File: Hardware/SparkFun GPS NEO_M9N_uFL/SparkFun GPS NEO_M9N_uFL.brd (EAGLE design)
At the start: 40.6 x 33 mm, 93 parts, among them J13 U.FL, J2 Qwiic Right Angle, J4 Qwiic Right Angle, U1 U-BLOX_NEO-M9N, U2 3.3V

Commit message: Adds sweet silk to NEO board
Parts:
- added U$21: (no value), NEO_GPS_board_silk_FINAL#03#jpg:NEO_GPS_BOARD_SILK_FINAL#03#JPG
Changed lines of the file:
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@@
 <element name="U$12" library="LEDs" package="PPS0" value="" x="39.878" y="9.652" smashed="yes" rot="MR0"/>
 <element name="U$17" library="LEDs" package="PWR1" value="" x="40.386" y="11.938" smashed="yes" rot="MR0"/>
+<element name="U$21" library="NEO_GPS_board_silk_FINAL#03#jpg" package="NEO_GPS_BOARD_SILK_FINAL#03#JPG" value="" x="15.24" y="11.43" smashed="yes" rot="MR0"/>
 </elements>
 <signals>

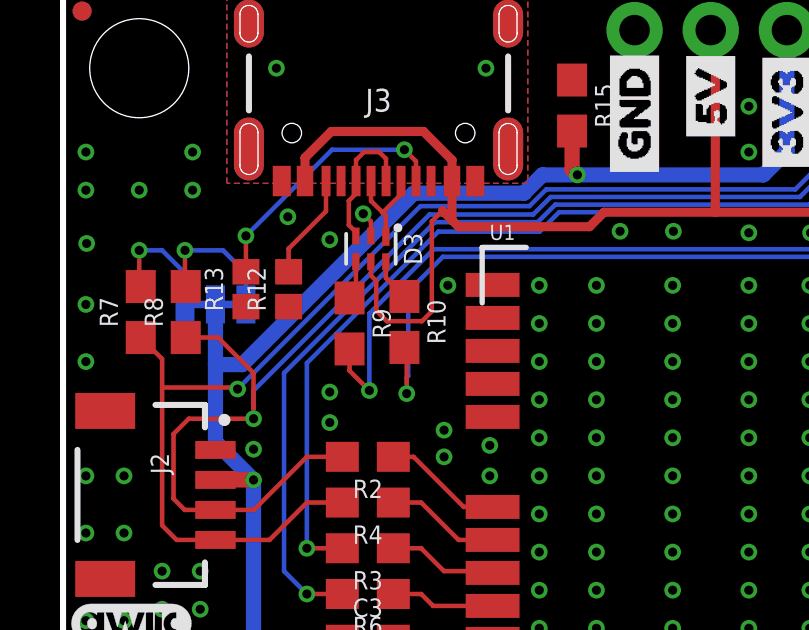
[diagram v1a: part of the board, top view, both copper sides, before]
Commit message: Updates both designs with 5.1k resistor in 0603 package
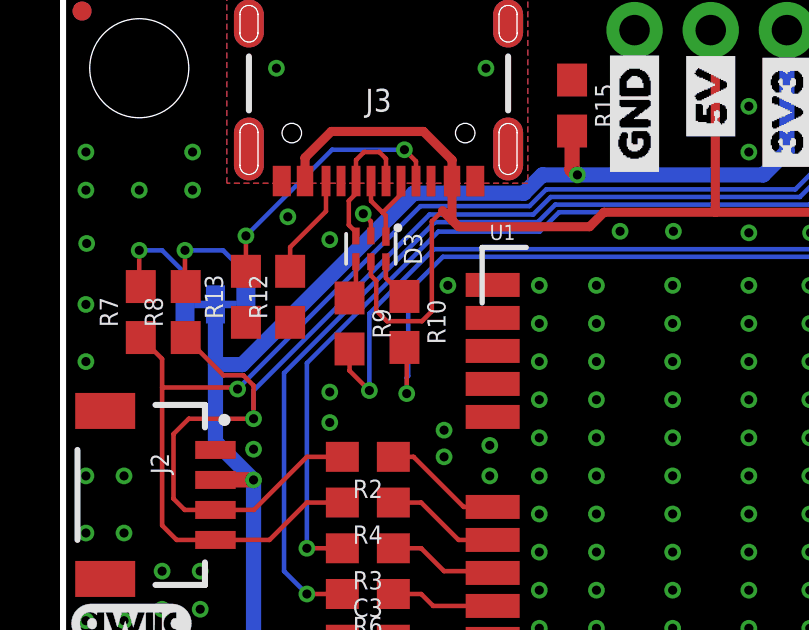
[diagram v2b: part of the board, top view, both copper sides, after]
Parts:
- R12, R13: device SparkFun-Resistors:0402 -> SparkFun-Resistors:0603
- moved R12 0.26 mm to (7.57, 22.8)
- moved R13 0.25 mm to (6.10, 22.8)
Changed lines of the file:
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@@
 <layer number="37" name="tTest" color="7" fill="1" visible="no" active="yes"/>
 <layer number="38" name="bTest" color="7" fill="1" visible="no" active="yes"/>
-<layer number="39" name="tKeepout" color="4" fill="11" visible="no" active="yes"/>
+<layer number="39" name="tKeepout" color="4" fill="11" visible="yes" active="yes"/>
 <layer number="40" name="bKeepout" color="1" fill="11" visible="no" active="yes"/>
 <layer number="41" name="tRestrict" color="4" fill="10" visible="no" active="yes"/>
@@
 <attribute name="VALUE" x="10.5156" y="30.6578" size="0.762" layer="27" rot="R180" align="center"/>
 </element>
-<element name="R12" library="SparkFun-Resistors" package="0402" value="5.1k" x="7.5184" y="23.0886" smashed="yes" rot="R90">
-<attribute name="NAME" x="6.7564" y="23.0886" size="0.6096" layer="25" font="vector" ratio="20" rot="R90" align="bottom-center"/>
-<attribute name="PROD_ID" value="RES-14340" x="7.5184" y="23.0886" size="1.778" layer="27" font="vector" ratio="15" rot="R90" display="off"/>
-<attribute name="VALUE" x="8.2804" y="23.0886" size="0.6096" layer="27" font="vector" ratio="20" rot="R90" align="top-center"/>
-</element>
-<element name="R13" library="SparkFun-Resistors" package="0402" value="5.1k" x="6.096" y="23.0886" smashed="yes" rot="R90">
-<attribute name="NAME" x="5.334" y="23.0886" size="0.6096" layer="25" font="vector" ratio="20" rot="R90" align="bottom-center"/>
-<attribute name="PROD_ID" value="RES-14340" x="6.096" y="23.0886" size="1.778" layer="27" font="vector" ratio="15" rot="R90" display="off"/>
-<attribute name="VALUE" x="6.858" y="23.0886" size="0.6096" layer="27" font="vector" ratio="20" rot="R90" align="top-center"/>
+<element name="R12" library="SparkFun-Resistors" package="0603" value="5.1k" x="7.5692" y="22.8346" smashed="yes" rot="R90">
+<attribute name="NAME" x="6.8072" y="22.8346" size="0.6096" layer="25" font="vector" ratio="20" rot="R90" align="bottom-center"/>
+<attribute name="PROD_ID" value="RES-12083" x="7.5692" y="22.8346" size="1.778" layer="27" font="vector" ratio="15" rot="R90" display="off"/>
+<attribute name="VALUE" x="8.3312" y="22.8346" size="0.6096" layer="27" font="vector" ratio="20" rot="R90" align="top-center"/>
+</element>
+<element name="R13" library="SparkFun-Resistors" package="0603" value="5.1k" x="6.096" y="22.8346" smashed="yes" rot="R90">
+<attribute name="NAME" x="5.334" y="22.8346" size="0.6096" layer="25" font="vector" ratio="20" rot="R90" align="bottom-center"/>
+<attribute name="PROD_ID" value="RES-12083" x="6.096" y="22.8346" size="1.778" layer="27" font="vector" ratio="15" rot="R90" display="off"/>
+<attribute name="VALUE" x="6.858" y="22.8346" size="0.6096" layer="27" font="vector" ratio="20" rot="R90" align="top-center"/>
 </element>
 <element name="R16" library="SparkFun-Resistors" package="0402" value="10k" x="29.718" y="10.414" smashed="yes" rot="R270">
@@
 <contactref element="J5" pad="3"/>
 <wire x1="31.4452" y1="3.5052" x2="29.21" y2="1.27" width="0.1524" layer="1"/>
-<wire x1="6.35" y1="20.2946" x2="5.168" y2="21.4766" width="0.1524" layer="1"/>
-<wire x1="6.35" y1="20.2946" x2="6.35" y2="18.7706" width="0.1524" layer="1"/>
 <wire x1="37.69396875" y1="16.493628125" x2="37.69396875" y2="14.477625" width="0.1524" layer="1"/>
 <wire x1="5.08" y1="15.7306" x2="4.056" y2="15.7306" width="0.1524" layer="1"/>
@@
 <wire x1="5.08" y1="15.7306" x2="6.358" y2="15.7306" width="0.1524" layer="1"/>
 <contactref element="R8" pad="1"/>
-<wire x1="5.168" y1="21.4766" x2="4.0894" y2="21.4766" width="0.1524" layer="1"/>
 <wire x1="26.67" y1="28.6766" x2="26.67" y2="28.2702" width="0.1524" layer="16"/>
 <wire x1="16.256" y1="26.162" x2="24.5618" y2="26.162" width="0.1524" layer="16"/>
 <wire x1="26.67" y1="28.2702" x2="24.5618" y2="26.162" width="0.1524" layer="16"/>
-<wire x1="12.21814375" y1="25.5778" x2="12.7" y2="25.5778" width="0.1524" layer="16"/>
-<wire x1="12.7" y1="25.5778" x2="15.6718" y2="25.5778" width="0.1524" layer="16"/>
+<wire x1="12.21814375" y1="25.5778" x2="15.6718" y2="25.5778" width="0.1524" layer="16"/>
 <wire x1="15.6718" y1="25.5778" x2="16.256" y2="26.162" width="0.1524" layer="16"/>
+<wire x1="4.0894" y1="21.4766" x2="5.3476" y2="20.2184" width="0.1524" layer="1"/>
+<wire x1="5.3476" y1="20.2184" x2="6.00746875" y2="20.2184" width="0.1524" layer="1"/>
+<wire x1="6.35" y1="19.87586875" x2="6.35" y2="18.7706" width="0.1524" layer="1"/>
+<wire x1="6.00746875" y1="20.2184" x2="6.35" y2="19.87586875" width="0.1524" layer="1"/>
 </signal>
 <signal name="!RESET">
@@
 <contactref element="J3" pad="B5"/>
 <wire x1="8.7656" y1="25.6862" x2="8.7656" y2="26.6938" width="0.1524" layer="1"/>
-<wire x1="7.5184" y1="23.6686" x2="7.5184" y2="24.439" width="0.1524" layer="1"/>
-<wire x1="7.5184" y1="24.439" x2="8.7656" y2="25.6862" width="0.1524" layer="1"/>
+<wire x1="7.5692" y1="23.6846" x2="7.5692" y2="24.4898" width="0.1524" layer="1"/>
+<wire x1="7.5692" y1="24.4898" x2="8.7656" y2="25.6862" width="0.1524" layer="1"/>
 </signal>
 <signal name="N$9">
@@
 <wire x1="8.9662" y1="27.7368" x2="6.096" y2="24.8666" width="0.1524" layer="16"/>
 <via x="6.096" y="24.8666" extent="1-16" drill="0.3048"/>
-<wire x1="6.096" y1="24.8666" x2="6.096" y2="23.6686" width="0.1524" layer="1"/>
+<wire x1="6.096" y1="24.8666" x2="6.096" y2="23.6846" width="0.1524" layer="1"/>
 </signal>
 </signals>

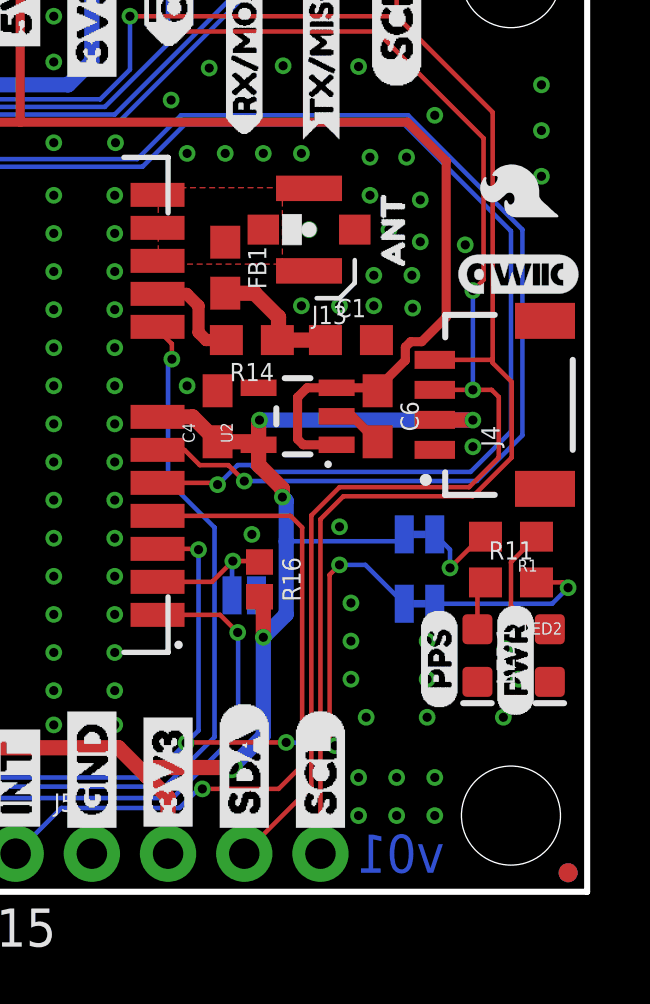
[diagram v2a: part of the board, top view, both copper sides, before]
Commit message: Updates Antenna silk
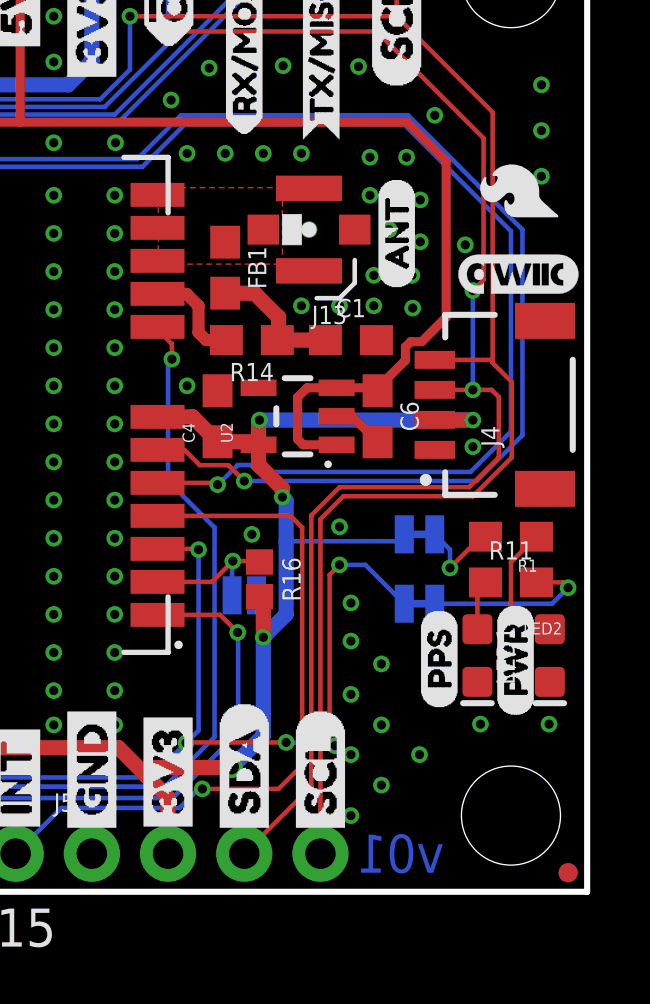
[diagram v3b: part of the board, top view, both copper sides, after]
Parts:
- removed U$55: (no value), buzzard_labels (9):ANT0
- added U$25: (no value), ANT:ANT0
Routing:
- net GND: vias 179 -> 174
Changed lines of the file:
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@@
 <layer number="37" name="tTest" color="7" fill="1" visible="no" active="yes"/>
 <layer number="38" name="bTest" color="7" fill="1" visible="no" active="yes"/>
-<layer number="39" name="tKeepout" color="4" fill="11" visible="yes" active="yes"/>
+<layer number="39" name="tKeepout" color="4" fill="11" visible="no" active="yes"/>
 <layer number="40" name="bKeepout" color="1" fill="11" visible="no" active="yes"/>
 <layer number="41" name="tRestrict" color="4" fill="10" visible="no" active="yes"/>
@@
 <element name="U$62" library="Labels" package="GND-04" value="" x="19.05" y="26.5176" smashed="yes" rot="MR90"/>
 <element name="U$63" library="Labels" package="GND-04" value="" x="19.05" y="26.5176" smashed="yes" rot="R90"/>
-<element name="U$55" library="buzzard_labels (9)" package="ANT0" value="" x="34.163" y="20.1676" smashed="yes" rot="R90"/>
 <element name="U$18" library="Labels" package="PWR-()-03" value="" x="38.2524" y="5.842" smashed="yes" rot="R90"/>
 <element name="J1" library="SparkFun-Connectors" package="1X07_NO_SILK" value="" x="19.05" y="31.7246" smashed="yes">
@@
 <element name="U$17" library="LEDs" package="PWR1" value="" x="40.386" y="11.938" smashed="yes" rot="MR0"/>
 <element name="U$21" library="NEO_GPS_board_silk_FINAL#03#jpg" package="NEO_GPS_BOARD_SILK_FINAL#03#JPG" value="" x="15.24" y="11.43" smashed="yes" rot="MR0"/>
+<element name="U$25" library="ANT" package="ANT0" value="" x="34.29" y="20.066" smashed="yes" rot="R90"/>
 </elements>
 <signals>
@@
 <via x="32.766" y="9.6266" extent="1-16" drill="0.3048"/>
 <via x="32.385" y="12.1666" extent="1-16" drill="0.3048"/>
-<via x="33.274" y="5.8166" extent="1-16" drill="0.3048"/>
-<via x="33.02" y="3.81" extent="1-16" drill="0.3048"/>
+<via x="32.766" y="6.5786" extent="1-16" drill="0.3048"/>
+<via x="32.766" y="4.572" extent="1-16" drill="0.3048"/>
 <via x="15.875" y="9.2456" extent="1-16" drill="0.3048"/>
 <via x="17.78" y="9.2456" extent="1-16" drill="0.3048"/>
@@
 <via x="31.369" y="22.0726" extent="1-16" drill="0.3048"/>
 <via x="27.305" y="16.8656" extent="1-16" drill="0.3048"/>
-<via x="33.02" y="2.54" extent="1-16" drill="0.3048"/>
-<via x="35.56" y="2.54" extent="1-16" drill="0.3048"/>
-<via x="35.56" y="3.81" extent="1-16" drill="0.3048"/>
-<via x="37.8968" y="8.1026" extent="1-16" drill="0.3048"/>
+<via x="32.766" y="2.54" extent="1-16" drill="0.3048"/>
+<via x="35.052" y="4.572" extent="1-16" drill="0.3048"/>
 <via x="6.858" y="2.54" extent="1-16" drill="0.3048"/>
 <via x="5.588" y="1.016" extent="1-16" drill="0.3048"/>
@@
 <via x="12.7" y="17.5006" extent="1-16" drill="0.3048"/>
 <via x="12.7" y="18.3896" extent="1-16" drill="0.3048"/>
-<via x="34.29" y="2.54" extent="1-16" drill="0.3048"/>
-<via x="34.29" y="3.81" extent="1-16" drill="0.3048"/>
+<via x="33.782" y="3.556" extent="1-16" drill="0.3048"/>
 <via x="32.766" y="8.3566" extent="1-16" drill="0.3048"/>
-<via x="35.306" y="8.3566" extent="1-16" drill="0.3048"/>
 <via x="3.302" y="13.6906" extent="1-16" drill="0.3048"/>
 <via x="4.572" y="13.6906" extent="1-16" drill="0.3048"/>
@@
 <via x="12.319" y="5.08" extent="1-16" drill="0.3048"/>
 <via x="8.509" y="4.572" extent="1-16" drill="0.3048"/>
-<via x="38.354" y="7.0866" extent="1-16" drill="0.3048"/>
-<via x="35.306" y="7.0866" extent="1-16" drill="0.3048"/>
-<via x="32.766" y="7.0866" extent="1-16" drill="0.3048"/>
-<via x="37.846" y="5.8166" extent="1-16" drill="0.3048"/>
-<via x="35.306" y="5.8166" extent="1-16" drill="0.3048"/>
+<via x="33.782" y="7.5946" extent="1-16" drill="0.3048"/>
+<via x="33.782" y="5.5626" extent="1-16" drill="0.3048"/>
 <via x="8.509" y="1.016" extent="1-16" drill="0.3048"/>
 <via x="12.319" y="1.016" extent="1-16" drill="0.3048"/>
@@
 <via x="30.5054" y="27.5336" extent="1-16" drill="0.3048"/>
 <via x="8.89" y="24.7396" extent="1-16" drill="0.3048"/>
+<via x="37.084" y="5.588" extent="1-16" drill="0.3048"/>
+<via x="39.37" y="5.588" extent="1-16" drill="0.3048"/>
 </signal>
 <signal name="SCL/SCK">

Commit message: Moves little bits around
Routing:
- net GND: vias 174 -> 171
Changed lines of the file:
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@@
 <contactref element="C1" pad="2"/>
 <via x="6.35" y="17.7546" extent="1-16" drill="0.3048"/>
-<via x="32.766" y="9.6266" extent="1-16" drill="0.3048"/>
 <via x="32.385" y="12.1666" extent="1-16" drill="0.3048"/>
-<via x="32.766" y="6.5786" extent="1-16" drill="0.3048"/>
-<via x="32.766" y="4.572" extent="1-16" drill="0.3048"/>
+<via x="32.766" y="7.3406" extent="1-16" drill="0.3048"/>
+<via x="32.766" y="4.826" extent="1-16" drill="0.3048"/>
 <via x="15.875" y="9.2456" extent="1-16" drill="0.3048"/>
 <via x="17.78" y="9.2456" extent="1-16" drill="0.3048"/>
@@
 <via x="14.224" y="16.8656" extent="1-16" drill="0.3048"/>
 <via x="14.224" y="17.8816" extent="1-16" drill="0.3048"/>
-<via x="12.7" y="17.5006" extent="1-16" drill="0.3048"/>
 <via x="12.7" y="18.3896" extent="1-16" drill="0.3048"/>
 <via x="33.782" y="3.556" extent="1-16" drill="0.3048"/>
-<via x="32.766" y="8.3566" extent="1-16" drill="0.3048"/>
+<via x="32.766" y="9.8806" extent="1-16" drill="0.3048"/>
 <via x="3.302" y="13.6906" extent="1-16" drill="0.3048"/>
 <via x="4.572" y="13.6906" extent="1-16" drill="0.3048"/>
@@
 <via x="12.319" y="5.08" extent="1-16" drill="0.3048"/>
 <via x="8.509" y="4.572" extent="1-16" drill="0.3048"/>
-<via x="33.782" y="7.5946" extent="1-16" drill="0.3048"/>
-<via x="33.782" y="5.5626" extent="1-16" drill="0.3048"/>
+<via x="33.782" y="8.6106" extent="1-16" drill="0.3048"/>
+<via x="33.782" y="6.3246" extent="1-16" drill="0.3048"/>
 <via x="8.509" y="1.016" extent="1-16" drill="0.3048"/>
 <via x="12.319" y="1.016" extent="1-16" drill="0.3048"/>
@@
 <via x="39.116" y="23.8506" extent="1-16" drill="0.3048"/>
 <via x="8.89" y="19.6596" extent="1-16" drill="0.3048"/>
-<via x="8.89" y="18.6436" extent="1-16" drill="0.3048"/>
 <via x="22.86" y="24.9682" extent="1-16" drill="0.3048"/>
 <via x="18.5674" y="25.019" extent="1-16" drill="0.3048"/>
